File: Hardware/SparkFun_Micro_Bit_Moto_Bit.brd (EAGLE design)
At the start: 76.2 x 58.4 mm, 48 parts, among them J1 5.5x2.1mm Barrel, J2 CORTEX_DEBUGPTH, J6 1X04_SMD_STRAIGHT_COMBO, U1 CY8C4245LQI-483, U2 TPS62172, U3 micro:bit, U4 DRV8835

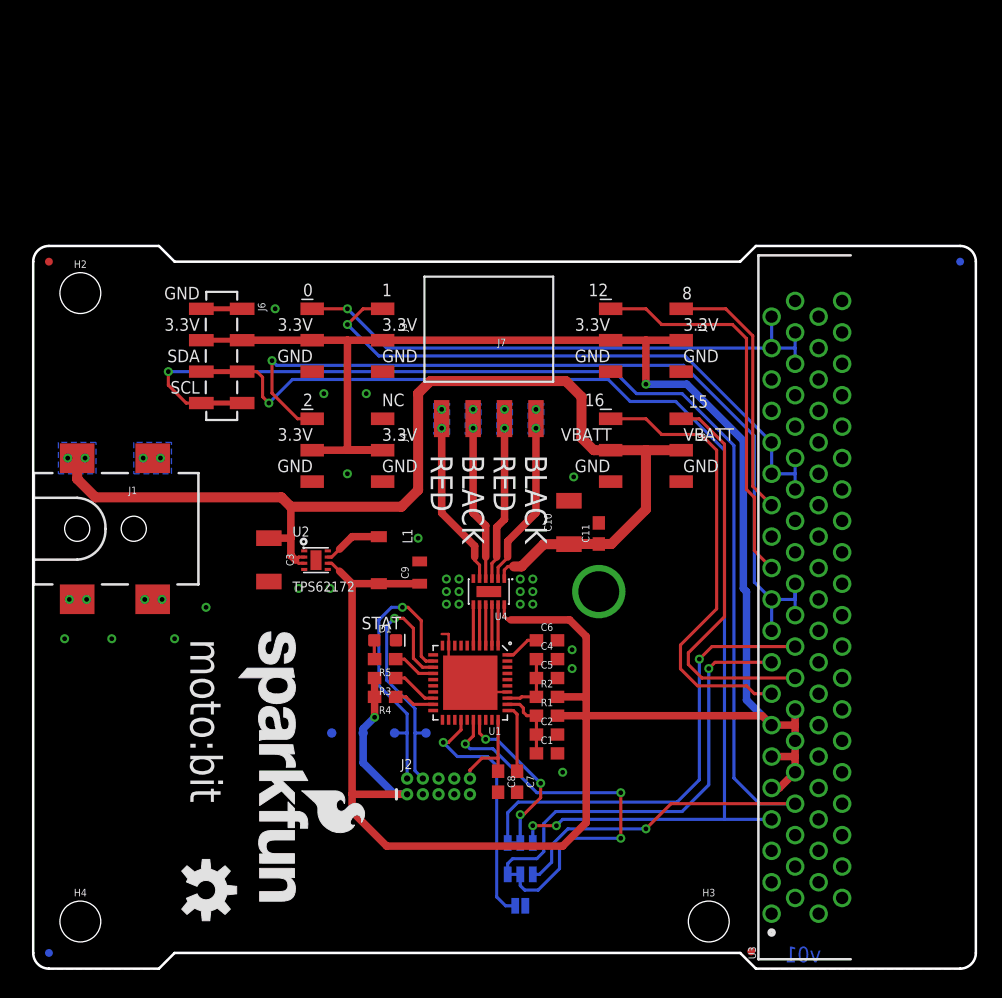
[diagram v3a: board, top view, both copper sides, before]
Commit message: Updated Changes
Made a bunch of changes based on suggestions from education
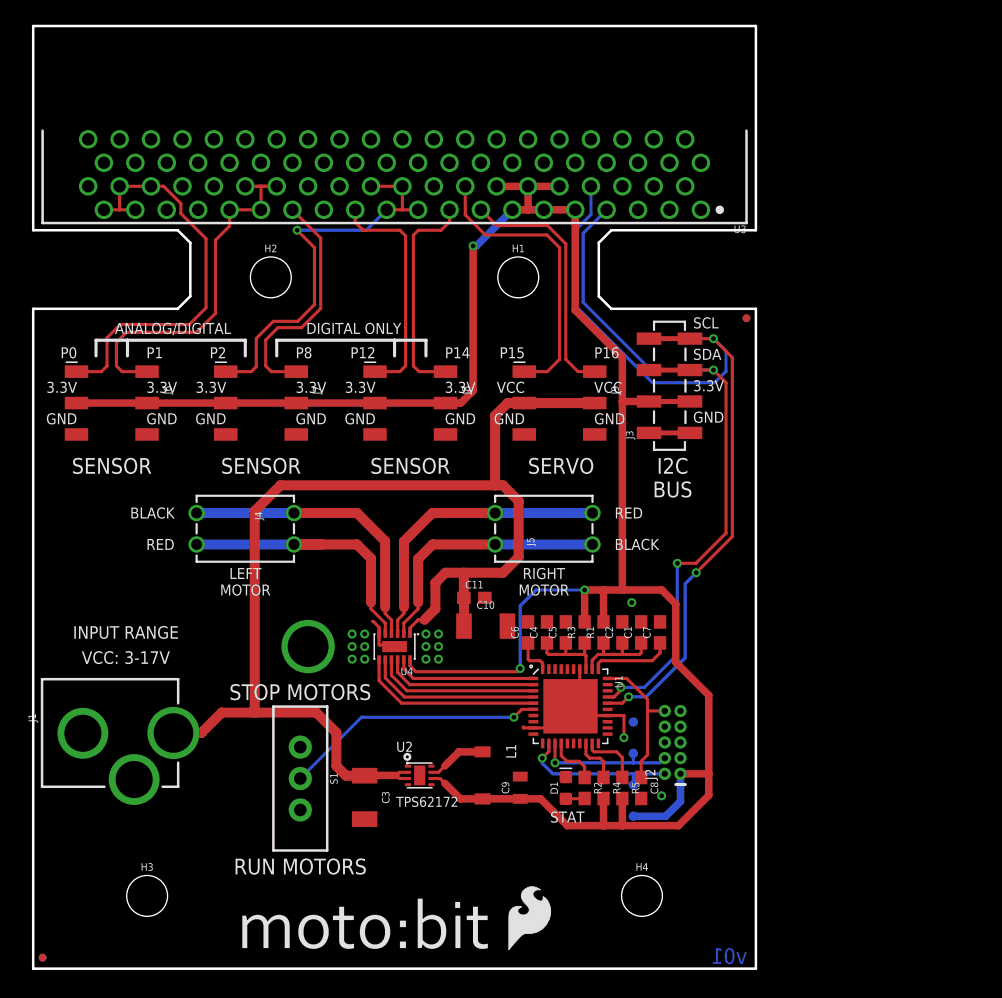
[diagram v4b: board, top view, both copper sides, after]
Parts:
- removed JP1, JP2: (no value), SparkFun-Jumpers:SMT-JUMPER_3_1-NC_TRACE_SILK
- removed JP3: (no value), SparkFun-Jumpers:SMT-JUMPER_2_NO_SILK
- added H1: STAND-OFF, SparkFun-Hardware:STAND-OFF
- added J9: (no value), SparkFun-Connectors:2X3_SMD
- added S1: (no value), SparkFun-Switches:SWITCH_SPDT_PTH_11.6X4.0MM
- added U$2: (no value), SparkFun-Aesthetics:SFE_LOGO_FLAME_.2
- added U$3: LOGO-MOTOBIT, Micro_Bit_Parts:LOGO-MOTOBIT
- J1: value 5.5x2.1mm Barrel -> POWER_JACKPTH_LOCK; device SparkFun-Connectors:POWER_JACK_SMD -> SparkFun-Connectors:POWER_JACK_PTH_LOCK
- J3: device SparkFun-Connectors:2X3_SMD -> SparkFun-Connectors:1X04_SMD_VERTICAL_COMBO
- J4, J5: device SparkFun-Connectors:2X3_SMD -> SparkFun-Connectors:1X02_RA_FEMALE
- J6: value 1X04_SMD_STRAIGHT_COMBO -> (none); device SparkFun-Connectors:1X04_SMD_VERTICAL_COMBO -> SparkFun-Connectors:2X3_SMD
- J7: device SparkFun-Connectors:1X04_SMD_RA_FEMALE -> SparkFun-Connectors:2X3_SMD
- L1: value 2.2µH/±20%/1.5A -> 2.2µH
- LOGO1: value SFE_LOGO_NAME_FLAME.2_INCH -> SFE_LOGO_NAME_FLAME.3_INCH; device SparkFun-Aesthetics:SFE_LOGO_NAME_FLAME_.2 -> SparkFun-Aesthetics:SFE_LOGO_NAME_FLAME_.3
- LOGO2: value OSHW-LOGOM -> OSHW-LOGOL; device SparkFun-Aesthetics:OSHW-LOGO-M -> SparkFun-Aesthetics:OSHW-LOGO-L
- R2: value 1 -> 470
- R3: value 4.7k -> 1
- R5: value 470 -> 4.7k
- moved FD3 93.1 mm to (0.76, 0.89)
- moved FD4 76.2 mm to (57.7, 52.6)
- moved FD1 57.3 mm to (0.76, 0.89)
- moved FD2 56.6 mm to (57.7, 52.6)
- moved U3 55.1 mm to (29.2, 69.0), turned to 180 degrees
- moved H3 45.4 mm to (9.21, 5.88)
- moved H4 45.4 mm to (49.2, 5.88)
- moved LOGO1 33.5 mm to (47.0, 41.9), flipped to the bottom, turned to 0 degrees
- moved J3 27.1 mm to (51.4, 43.3), turned to 90 degrees
- moved TP4 24.4 mm to (48.5, 19.9), turned to 270 degrees
- moved TP3 22.9 mm to (48.5, 12.3), turned to 270 degrees
- moved R5 21.8 mm to (47.6, 14.6), turned to 270 degrees
- moved C3 20.7 mm to (26.8, 13.8)
- moved TP1 19.8 mm to (48.5, 14.9), turned to 270 degrees
- moved J8 19.4 mm to (30.5, 45.7)
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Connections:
- removed net P0.2: JP3.2, U1.24
- removed net P0.4: JP1.2, U1.26
- removed net P0.5: JP2.2, U1.27
- removed net V_BATT: C10.1, C11.1, C3.1, J1.VIN0, J8.3, J8.4, U2.2, U2.3, U4.1
- new net U2.5: S1.2, U1.6
- new net VCC: C10.1, C11.1, C3.1, J1.PWR, J9.3, J9.4, U2.2, U2.3, U4.1
- net 3.3V: now also J3.2, J6.3, J6.4, J7.3, J7.4, J8.3, J8.4, R5.2; no longer J3.3, J3.4, J4.3, J4.4, J5.3, J5.4, J6.2, R2.2
- net ANALOG_0: now also J6.1; no longer J3.1
- net ANALOG_1: now also J6.2; no longer J3.2
- net ANALOG_2: now also J7.1; no longer J4.1
- net AO1: now also J5.P$1, J5.P$3; no longer J7.1
- net AO2: now also J5.P$2, J5.P$4; no longer J7.2
- net BO1: now also J4.P$1, J4.P$3; no longer J7.3
- net BO2: now also J4.P$2, J4.P$4; no longer J7.4
- net DIGITAL_12: now also J8.1; no longer J5.1
- net DIGITAL_8: now also J7.2; no longer J5.2
- net GND: now also J1.GNDBREAK, J3.1, J6.5, J6.6, J7.5, J7.6, J9.5, J9.6, S1.3, U1.24; no longer J1.P$4, J3.5, J3.6, J4.5, J4.6, J5.5, J5.6, J6.1, JP3.1
- net N$3: now also R3.1; no longer R2.1
- net N$6: now also R4.1; no longer R3.1
- net N$7: now also R5.1; no longer R4.1
- net N$8: now also R2.2; no longer R5.2
- net RX: now also J8.2; no longer JP1.3
- net SCL: now also J3.4, U1.26; no longer J6.4, JP1.1
- net SDA: now also J3.3, U1.27; no longer J6.3, JP2.1
- net SERVO_15: now also J9.1; no longer J8.2
- net SERVO_16: now also J9.2; no longer J8.1
- net SLED: now also R2.1; no longer R5.1
- net TX: no longer JP2.3
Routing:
- net VCC: track 0.00 -> 99.3 mm
- net V_BATT: track 93.4 -> 0.00 mm, vias 2 -> 0
- net SCL: track 112.9 -> 69.3 mm, vias 2 -> 3
- net SDA: track 98.2 -> 56.1 mm
- net ANALOG_2: track 70.3 -> 32.2 mm
- net TX: track 37.0 -> 0.00 mm, vias 1 -> 0
- net P0.4: track 32.0 -> 0.00 mm, vias 3 -> 0
- net 3.3V: track 209.1 -> 183.4 mm, vias 2 -> 3
- net U2.5: track 0.00 -> 21.2 mm, vias 0 -> 1
- net P0.2: track 20.2 -> 0.00 mm, vias 1 -> 0
- net RX: track 35.8 -> 17.7 mm, vias 1 -> 0
- net ANALOG_1: track 48.6 -> 31.0 mm, vias 1 -> 0
- net SERVO_16: track 36.7 -> 20.1 mm
- net P0.5: track 13.4 -> 0.00 mm, vias 3 -> 0
- net DIGITAL_12: track 31.4 -> 18.7 mm
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- removed copper zone on layer 16, net AO1
- removed copper zone on layer 16, net AO2
- removed copper zone on layer 16, net BO1
- removed copper zone on layer 16, net BO2
- removed copper zone on layer 16, net N$5
- removed copper zone on layer 16, net V_BATT
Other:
- board size 76.2 x 58.4 mm -> 58.4 x 76.2 mm
- board text added: "- Solder mask color : Black"
- board text added: "ANALOG/DIGITAL"
- board text added: "DIGITAL ONLY"
- board text added: "I2C BUS"
- board text added: "INPUT RANGE"
- board text added: "LEFT MOTOR"
- board text added: "P0"
- board text added: "P1"
- board text added: "P12"
- board text added: "P14"
- board text added: "P15"
- board text added: "P16"
- board text added: "P2"
- board text added: "P8"
- board text added: "RIGHT MOTOR"
- board text added: "RUN MOTORS"
- board text added: "SENSOR"
- board text added: "SERVO"
- board text added: "STOP MOTORS"
- board text added: "VCC"
- board text added: "VCC: 3-17V"
- board text added: "sparkfun.com/microbit"
- board text removed: "- Solder mask color : Black (Gloss if available)"
- board text removed: "0"
- board text removed: "0x59"
- board text removed: "1"
- board text removed: "12"
- board text removed: "15"
- board text removed: "16"
- board text removed: "2"
- board text removed: "8"
- board text removed: "I2C"
- board text removed: "NC"
- board text removed: "UART"
- board text removed: "Units are in inches"
- board text removed: "VBATT"

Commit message: Updated Measures Layer
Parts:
- U$3: value LOGO-MOTOBIT -> (none)
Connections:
- net RX renamed DIGITAL_14
- removed net TX: U3.A18
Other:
- board text added: "- Solder mask color : Gloss Black"
- board text added: "Units are in Inches"
- board text removed: "- Solder mask color : Black"
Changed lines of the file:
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@@
 <layer number="20" name="Dimension" color="15" fill="1" visible="yes" active="yes"/>
 <layer number="21" name="tPlace" color="16" fill="1" visible="yes" active="yes"/>
-<layer number="22" name="bPlace" color="14" fill="1" visible="no" active="yes"/>
+<layer number="22" name="bPlace" color="14" fill="1" visible="yes" active="yes"/>
 <layer number="23" name="tOrigins" color="15" fill="1" visible="yes" active="yes"/>
 <layer number="24" name="bOrigins" color="15" fill="1" visible="yes" active="yes"/>
@@
 <layer number="43" name="vRestrict" color="2" fill="10" visible="no" active="yes"/>
 <layer number="44" name="Drills" color="7" fill="1" visible="no" active="yes"/>
-<layer number="45" name="Holes" color="7" fill="1" visible="no" active="yes"/>
+<layer number="45" name="Holes" color="7" fill="1" visible="yes" active="yes"/>
 <layer number="46" name="Milling" color="3" fill="1" visible="no" active="yes"/>
 <layer number="47" name="Measures" color="7" fill="1" visible="yes" active="yes"/>
-<layer number="48" name="Document" color="7" fill="1" visible="yes" active="yes"/>
+<layer number="48" name="Document" color="7" fill="1" visible="no" active="yes"/>
 <layer number="49" name="Reference" color="7" fill="1" visible="no" active="yes"/>
 <layer number="50" name="dxf" color="7" fill="1" visible="no" active="no"/>
@@
 <text x="24.13" y="-31.75" size="1.778" layer="51" font="vector" ratio="15">Alex Wende</text>
 <text x="56.261" y="0.381" size="1.27" layer="16" font="vector" ratio="15" rot="MR0" align="bottom-center">v01</text>
-<text x="-17.78" y="-49.53" size="1.27" layer="51" font="vector" ratio="15">- Solder mask color : Black</text>
+<text x="-17.78" y="-49.53" size="1.27" layer="51" font="vector" ratio="15">- Solder mask color : Gloss Black</text>
 <wire x1="0" y1="0" x2="58.42" y2="0" width="0.2032" layer="20"/>
-<polygon width="0.2032" layer="51">
-<vertex x="6.985" y="0"/>
-<vertex x="10.16" y="0"/>
-<vertex x="10.16" y="-4.064"/>
-<vertex x="6.985" y="-4.064"/>
-</polygon>
-<polygon width="0.2032" layer="51">
-<vertex x="47.625" y="0"/>
-<vertex x="50.8" y="0"/>
-<vertex x="50.8" y="-4.064"/>
-<vertex x="47.625" y="-4.064"/>
-</polygon>
-<polygon width="0.2032" layer="51">
-<vertex x="6.985" y="57.531"/>
-<vertex x="10.16" y="57.531"/>
-<vertex x="10.16" y="53.594"/>
-<vertex x="6.985" y="53.594"/>
-</polygon>
-<polygon width="0.2032" layer="51">
-<vertex x="47.625" y="57.531"/>
-<vertex x="50.8" y="57.531"/>
-<vertex x="50.8" y="53.594"/>
-<vertex x="47.625" y="53.594"/>
-</polygon>
 <wire x1="58.42" y1="59.69" x2="46.736" y2="59.69" width="0.2032" layer="20"/>
 <wire x1="46.736" y1="59.69" x2="45.72" y2="58.674" width="0.2032" layer="20"/>
@@
 <wire x1="7.62" y1="50.8" x2="7.62" y2="49.53" width="0.254" layer="21"/>
 <wire x1="5.08" y1="50.8" x2="5.08" y2="49.53" width="0.254" layer="21"/>
+<dimension x1="9.21" y1="5.88" x2="9.21" y2="0" x3="-5.065384375" y3="2.94" textsize="1.016" textratio="15" layer="47" unit="inch" precision="3"/>
+<dimension x1="19.21" y1="55.88" x2="19.21" y2="53.34" x3="-5.076546875" y3="54.61" textsize="1.016" textratio="15" layer="47" unit="inch" precision="3"/>
+<dimension x1="9.21" y1="5.88" x2="9.21" y2="53.34" x3="-5.063315625" y3="29.61" textsize="1.016" textratio="15" layer="47" unit="inch" precision="3"/>
+<dimension x1="0" y1="59.69" x2="0" y2="76.2" x3="-2.54" y3="67.945" textsize="1.016" textratio="15" layer="47" unit="inch" precision="3"/>
+<dimension x1="19.21" y1="55.88" x2="0" y2="55.88" x3="9.605" y3="78.74" textsize="1.016" textratio="15" layer="47" unit="inch" precision="3"/>
+<dimension x1="19.21" y1="55.88" x2="39.21" y2="55.88" x3="29.21" y3="78.74" textsize="1.016" textratio="15" layer="47" unit="inch" precision="3"/>
+<dimension x1="39.21" y1="55.88" x2="58.42" y2="55.88" x3="48.815" y3="78.74" textsize="1.016" textratio="15" layer="47" unit="inch" precision="3"/>
+<dimension x1="0" y1="0" x2="58.42" y2="0" x3="29.21" y3="-6.35" textsize="1.016" textratio="15" layer="47" unit="inch" precision="3"/>
+<dimension x1="58.42" y1="0" x2="58.42" y2="76.2" x3="63.5" y3="38.1" textsize="1.016" textratio="15" layer="47" unit="inch" precision="3"/>
+<dimension x1="9.21" y1="5.88" x2="0" y2="5.88" x3="4.605" y3="-2.560265625" textsize="1.016" textratio="15" layer="47" unit="inch" precision="3"/>
+<dimension x1="9.21" y1="5.88" x2="49.21" y2="5.88" x3="29.21" y3="-2.54" textsize="1.016" textratio="15" layer="47" unit="inch" precision="3"/>
+<dimension x1="49.21" y1="5.88" x2="58.42" y2="5.88" x3="53.815" y3="-2.563565625" textsize="1.016" textratio="15" layer="47" unit="inch" precision="3"/>
+<dimension x1="58.42" y1="59.69" x2="58.42" y2="53.34" x3="60.96" y3="56.515" textsize="1.016" textratio="15" layer="47" unit="inch" precision="3"/>
+<text x="13.97" y="-10.16" size="1.778" layer="47" font="vector" ratio="15">Units are in Inches</text>
 </plain>
 <attributes>
@@
 <attribute name="SF_SKU" value="COM-00102" x="21.59" y="15.367" size="1.778" layer="27" font="vector" ratio="15" rot="R180" display="off"/>
 </element>
-<element name="U$3" library="Micro_Bit_Parts" package="LOGO-MOTOBIT" value="LOGO-MOTOBIT" x="16.764" y="1.27"/>
+<element name="U$3" library="Micro_Bit_Parts" package="LOGO-MOTOBIT" value="" x="16.764" y="1.27"/>
 </elements>
 <signals>
@@
 <wire x1="11.938" y1="61.040028125" x2="13.97" y2="59.008028125" width="0.254" layer="1"/>
 </signal>
-<signal name="RX">
+<signal name="DIGITAL_14">
 <contactref element="U3" pad="A17"/>
 <contactref element="J8" pad="2"/>
@@
 <wire x1="32.971084375" y1="59.69" x2="31.13560625" y2="59.69" width="0.254" layer="1"/>
 </signal>
-<signal name="TX">
-<contactref element="U3" pad="A18"/>
-</signal>
 <signal name="SERVO_16">

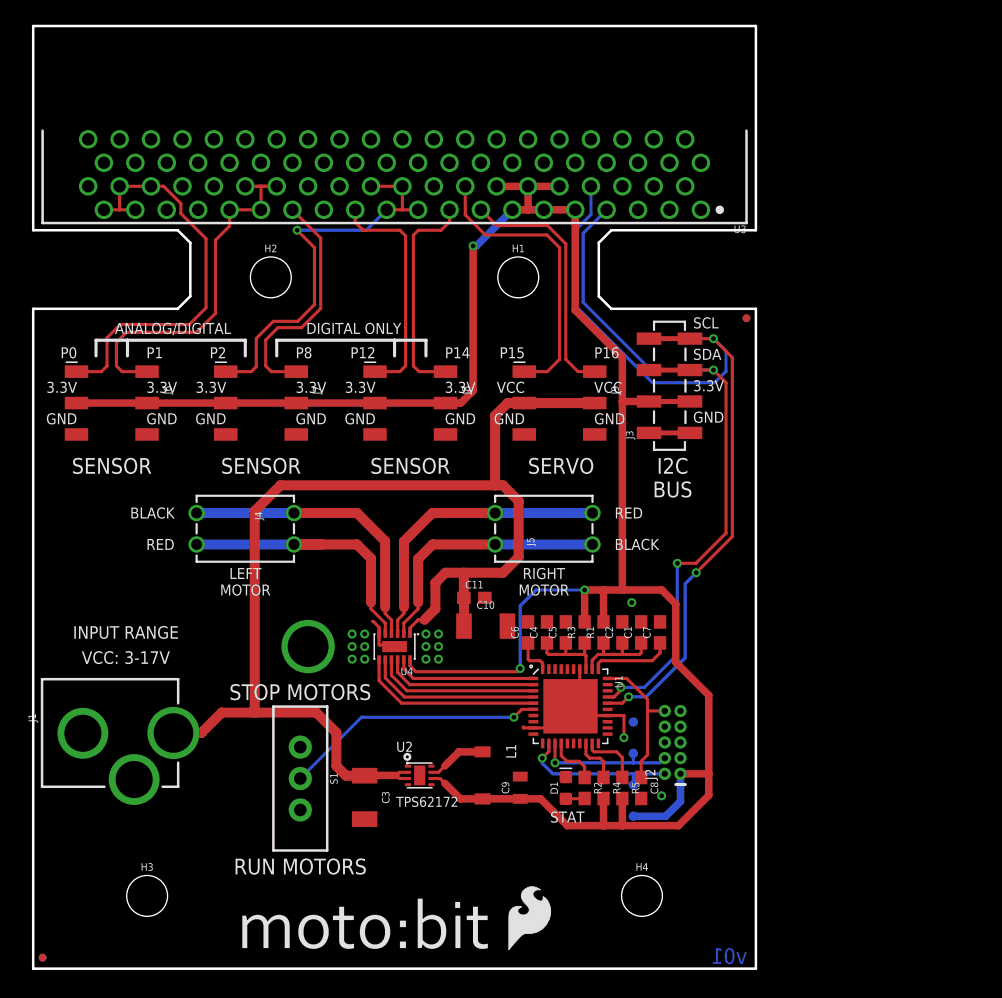
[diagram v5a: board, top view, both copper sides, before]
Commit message: Design review changes
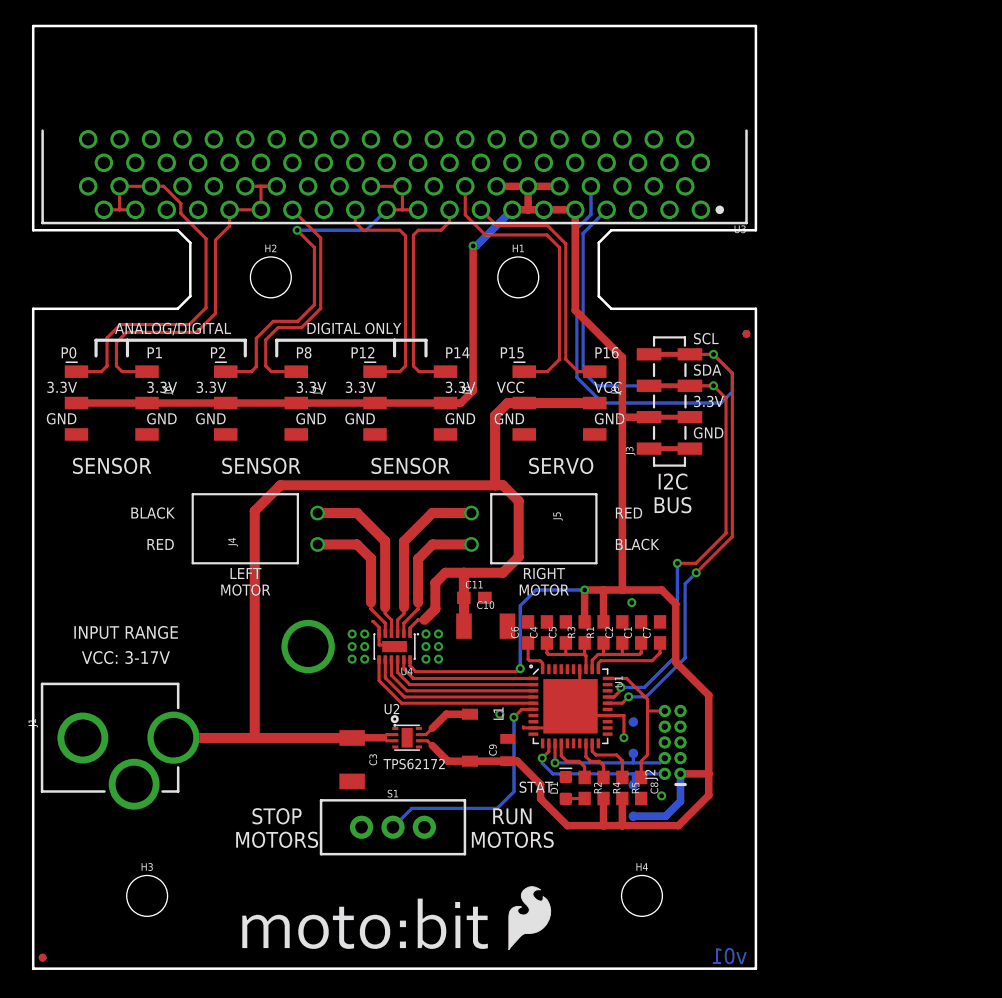
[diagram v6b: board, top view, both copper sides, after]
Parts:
- added U$4: (no value), Micro_Bit_Parts:LOGO-MOTOBIT
- moved S1 8.46 mm to (29.1, 11.4), turned to 270 degrees
- moved LOGO2 7.49 mm to (29.1, 6.48)
- moved L1 3.21 mm to (35.3, 18.7)
- moved U2 3.21 mm to (30.2, 18.7)
- moved C9 3.21 mm to (38.4, 17.7)
- moved C3 3.21 mm to (25.8, 16.9)
- moved FD2 1.27 mm to (57.7, 51.3)
- moved FD4 1.27 mm to (57.7, 51.3)
- moved J3 1.27 mm to (51.4, 42.0)
- moved J1 0.38 mm to (-2.54, 18.7)
- turned J4 to 90 degrees
- turned J5 to 270 degrees
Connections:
- net AO1: now also J5.1; no longer J5.P$1, J5.P$3
- net AO2: now also J5.2; no longer J5.P$2, J5.P$4
- net BO1: now also J4.1; no longer J4.P$1, J4.P$3
- net BO2: now also J4.2; no longer J4.P$2, J4.P$4
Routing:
- net BO2: track 23.4 -> 11.3 mm
- net AO2: track 23.9 -> 14.1 mm
- net AO1: track 21.1 -> 11.3 mm
- net BO1: track 23.9 -> 14.1 mm
- net SCL: track 69.3 -> 73.1 mm
- net VCC: track 99.3 -> 96.0 mm
- net 3.3V: track 183.4 -> 186.4 mm
- net SDA: track 56.1 -> 58.6 mm
- net U2.5: track 21.2 -> 18.8 mm
- net GND: vias 15 -> 16
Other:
- board text removed: "moto:bit"
